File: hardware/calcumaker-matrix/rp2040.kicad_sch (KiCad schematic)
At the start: 22 parts, among them J4 USB-C (BOOTSEL), SW1 BOOTSEL, U1 RP2040, U2 W25Q32JVSSIQ, U3 USBLC6-2SC6, Y1 12MHz

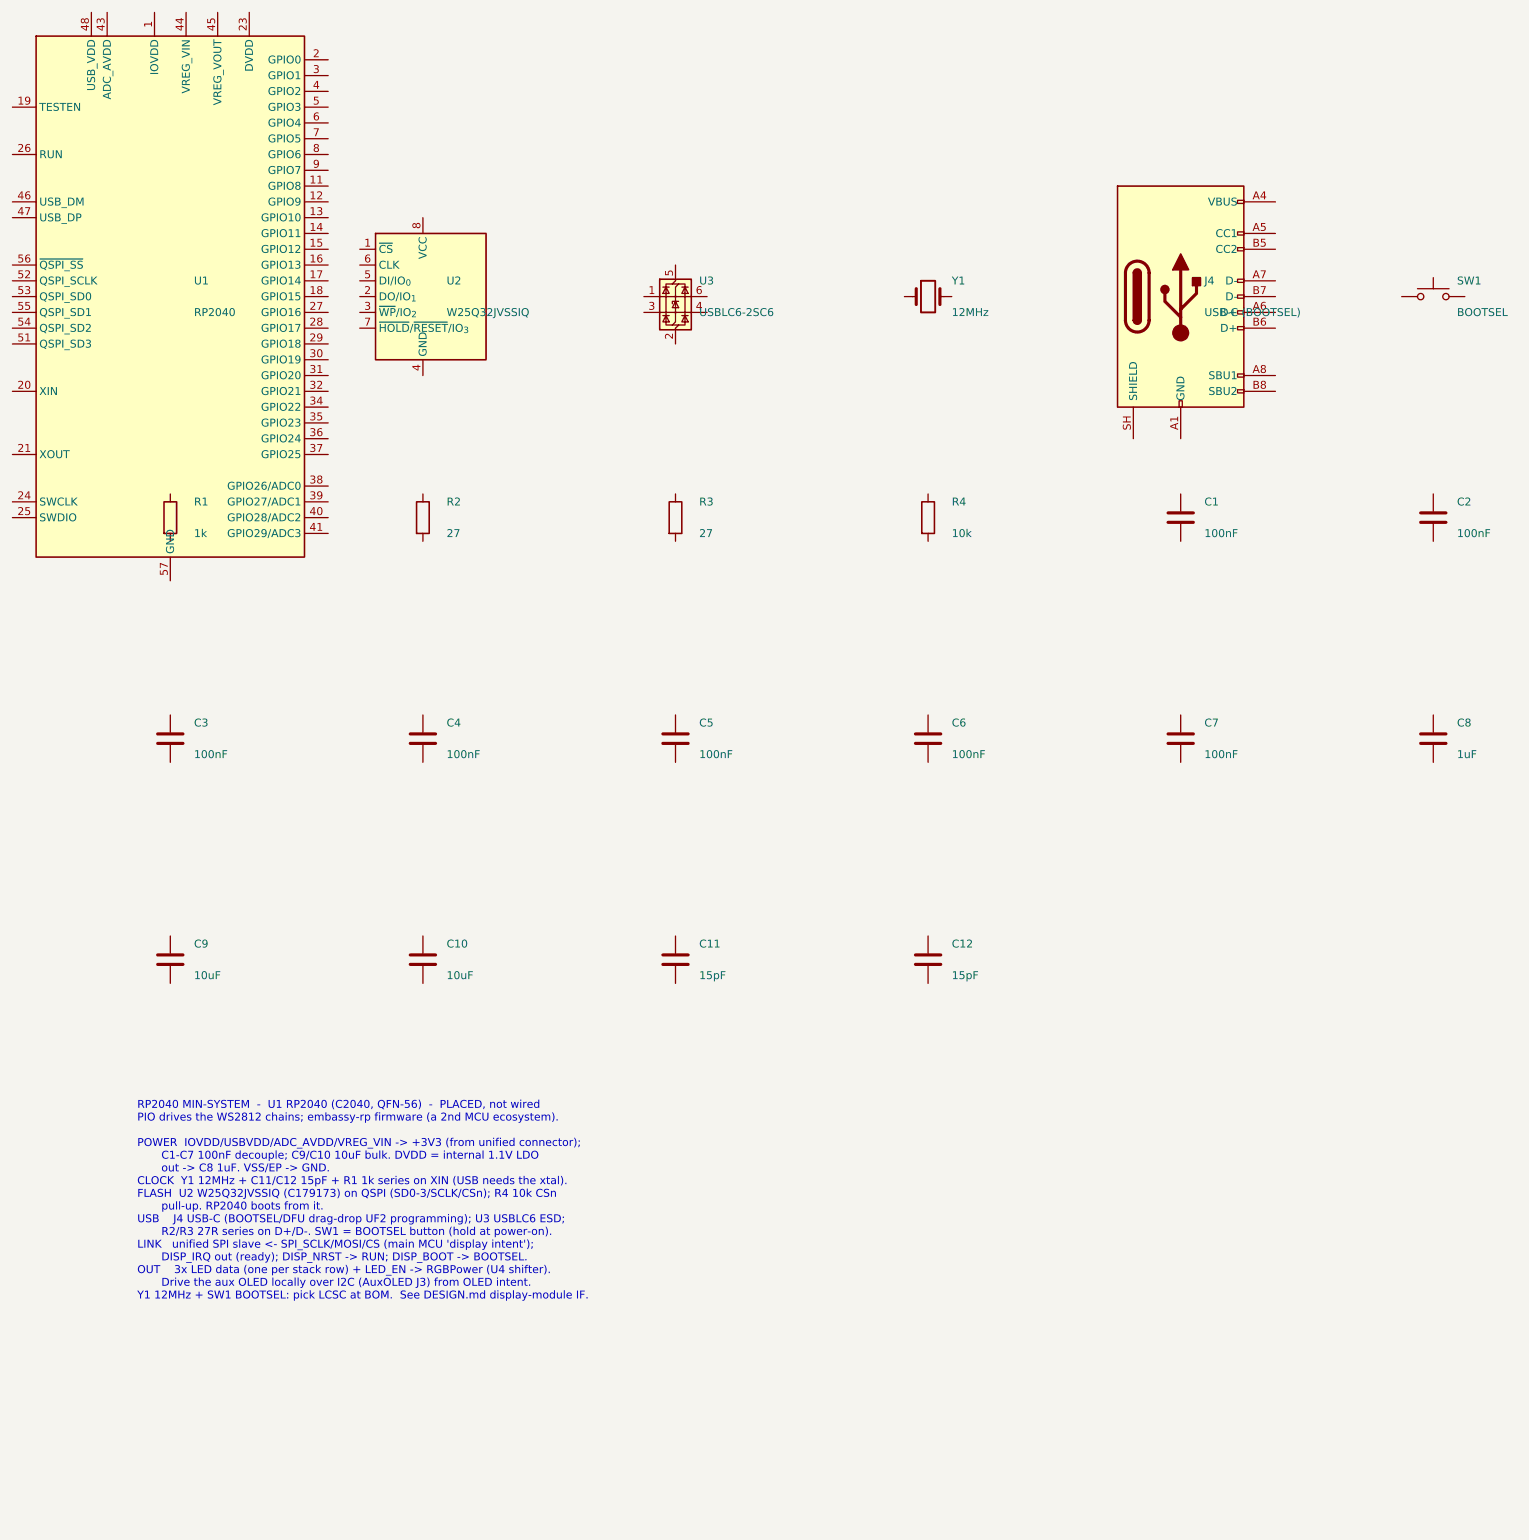
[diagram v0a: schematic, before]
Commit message: firmware: scaffold the two display-module targets + wire the module sheets
Firmware scaffold (all build; targets thumbv6m-none-eabi):
- calcumaker-display-proto: shared no_std wire protocol — the "display intent"
  DisplayFrame the U575 sends over SPI (text rows + flags + aux), with a
  fixed-length checksummed codec. Host-tested (cargo test: 3/3).
- calcumaker-display-fw: 7-seg module (STM32G031, embassy-stm32) — SPI-slave
  receiver + a bit-bang TM1640 driver + 7-seg render.
- calcumaker-matrix-fw: RGB-matrix module (RP2040, embassy-rp) — SPI-slave
  receiver + a 96x24 framebuffer/font blitter; WS2812 PIO output + SPI DMA
  stubbed as the bring-up TODOs.

Wire the one-off module schematic sheets (were placed-not-wired):
- kschgen: pin_geom now follows (extends ...) like pin_numbers, so derived
  symbols (STM32G031, 74xx) wire via net_pin.
- matrix rp2040 + rgb_power: RP2040 power/clock/flash/USB + the FET load switch
  and 3x single-gate level shifters are fully wired.
- display disp_mcu + disp_power: STM32G031 + the TPS61022 boost and 4x single-
  gate shifters are fully wired. (Quad 74xx buffers were multi-unit, which
  kschgen can't place fully, so the shifters are single-gate 74x1G125 — matching
  the keyboard's approach.)

All 4 boards check clean (mcu 46 / keyboard 179 / display 83 / matrix 2343, no
dup refs); wiring cut ERC pin_not_connected ~4x on both display modules.

Co-Authored-By: Claude Opus 4.8 (1M context) <noreply@anthropic.com>
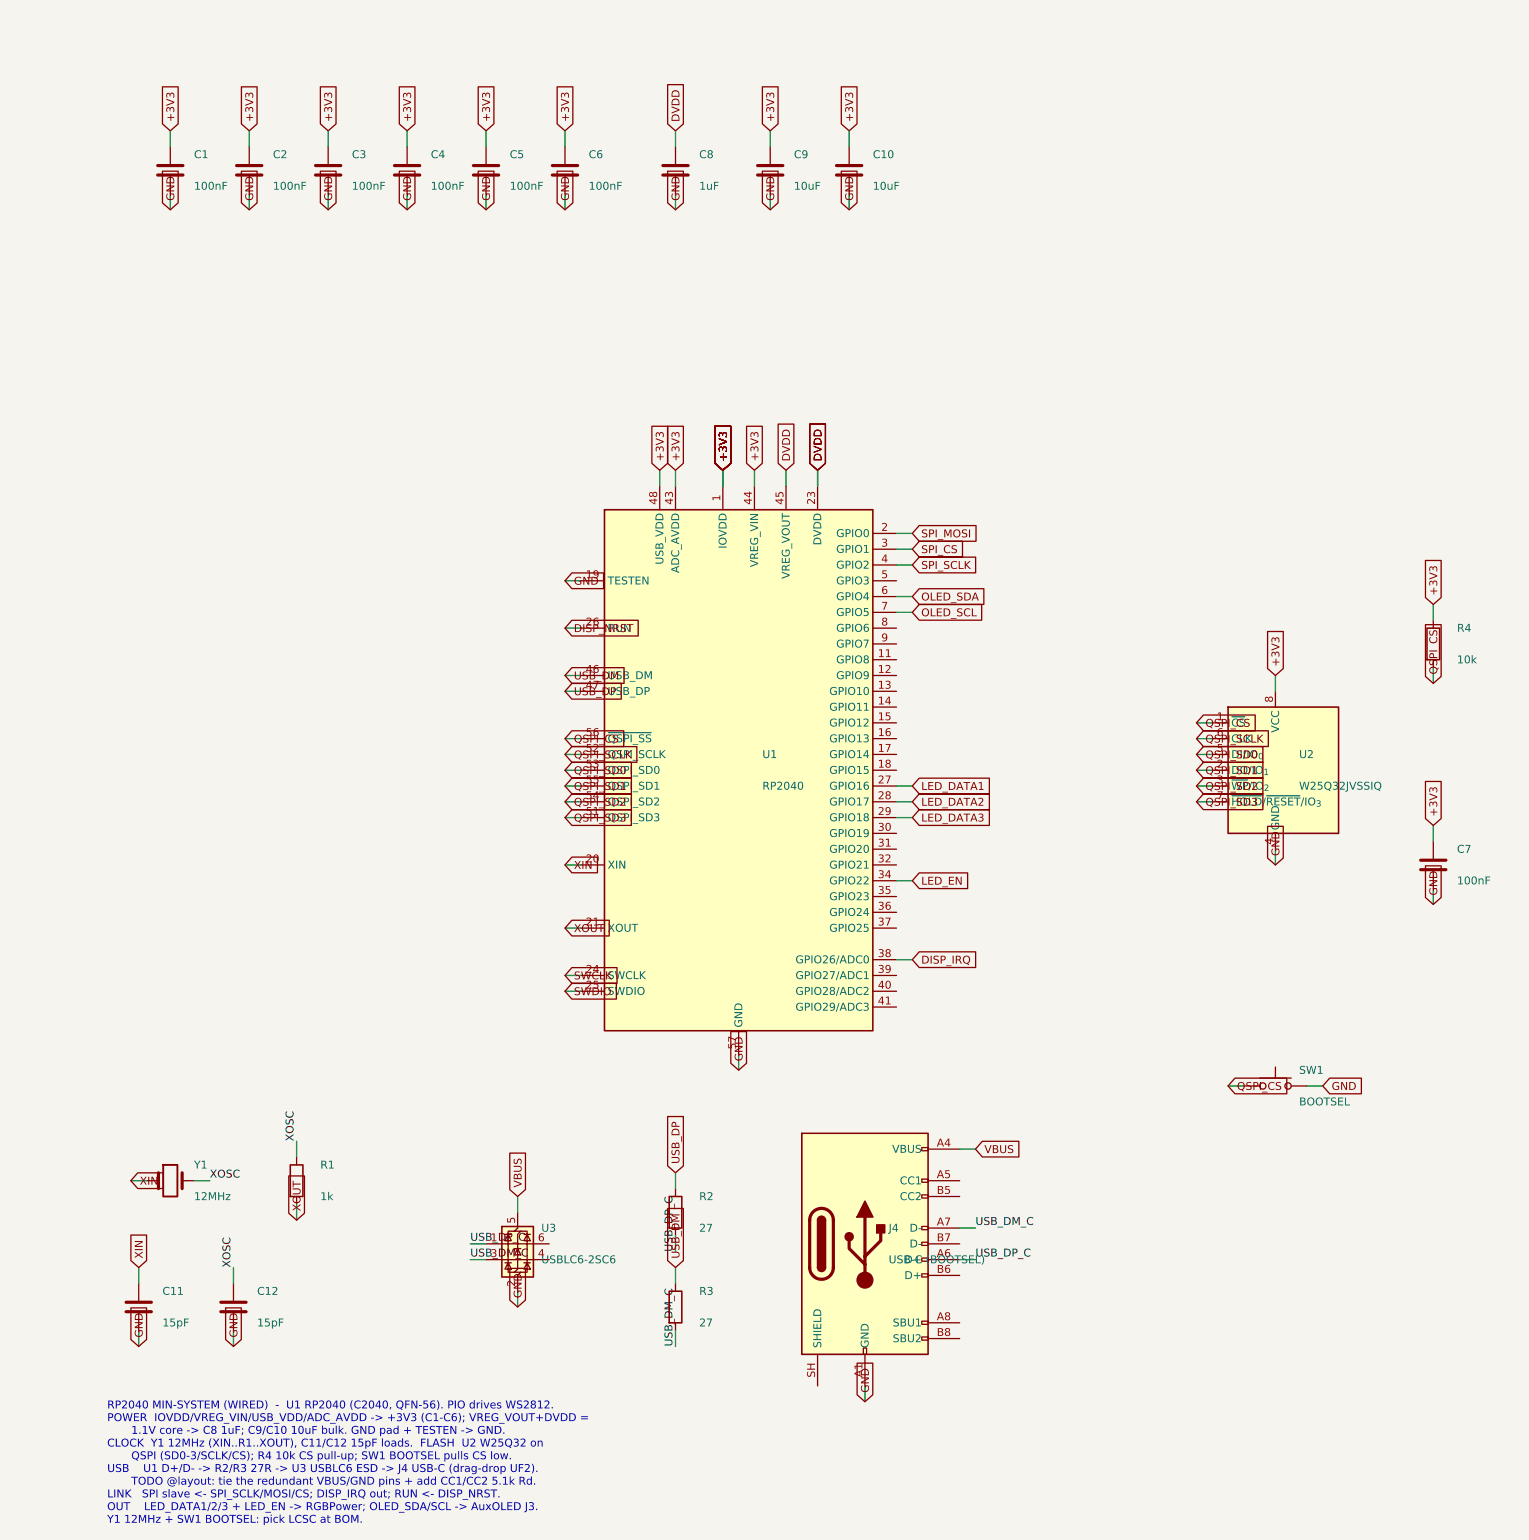
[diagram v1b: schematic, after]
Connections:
- net QSPI_CS: now reaches U2.1 (~{CS})
- net QSPI_CS: now also R4.2, SW1.1, U1.56 (~{QSPI_SS})
- net QSPI_SD1: now reaches U2.2 (DO/IO_{1})
- net QSPI_SD1: now also U1.55 (QSPI_SD1)
- net QSPI_SD2: now reaches U2.3 (~{WP}/IO_{2})
- net QSPI_SD2: now also U1.54 (QSPI_SD2)
- net GND: now reaches U2.4 (GND)
- net GND: now also C1.2, C10.2, C11.2, C12.2, C2.2, C3.2, C4.2, C5.2, C6.2, C7.2, C8.2, C9.2, J4.A1 (GND), J4.A12 (GND), J4.B1 (GND), J4.B12 (GND), SW1.2, U1.19 (TESTEN), U1.57 (GND), U3.2 (GND)
- net QSPI_SD0: now reaches U2.5 (DI/IO_{0})
- net QSPI_SD0: now also U1.53 (QSPI_SD0)
- net QSPI_SCLK: now reaches U2.6 (CLK)
- net QSPI_SCLK: now also U1.52 (QSPI_SCLK)
- net QSPI_SD3: now reaches U2.7 (~{HOLD}/~{RESET}/IO_{3})
- net QSPI_SD3: now also U1.51 (QSPI_SD3)
- net +3V3: now reaches U2.8 (VCC)
- net +3V3: now also C1.1, C10.1, C2.1, C3.1, C4.1, C5.1, C6.1, C7.1, C9.1, R4.1, U1.1 (IOVDD), U1.10 (IOVDD), U1.22 (IOVDD), U1.33 (IOVDD), U1.42 (IOVDD), U1.43 (ADC_AVDD), U1.44 (VREG_VIN), U1.48 (USB_VDD), U1.49 (IOVDD)
- net XIN: now reaches Y1.1
- net XIN: now also C11.1, U1.20 (XIN)
- net XOSC: now reaches Y1.2
- net XOSC: now also C12.1, R1.1
- net USB_DP: now reaches R2.1
- net USB_DP: now also U1.47 (USB_DP)
- net USB_DP_C: now reaches R2.2
- net USB_DP_C: now also J4.A6 (D+), U3.1 (I/O1)
- net USB_DM_C: now reaches U3.3 (I/O2)
- net USB_DM_C: now also J4.A7 (D-), R3.2
- net VBUS: now reaches U3.5 (VBUS)
- net VBUS: now also J4.A4 (VBUS), J4.A9 (VBUS), J4.B4 (VBUS), J4.B9 (VBUS)
- net SPI_MOSI: now reaches U1.2 (GPIO0)
- net XOUT: now reaches U1.21 (XOUT)
- net XOUT: now also R1.2
- net DVDD: now reaches U1.23 (DVDD), U1.50 (DVDD)
- net DVDD: now also C8.1, U1.45 (VREG_VOUT)
- net SWCLK: now reaches U1.24 (SWCLK)
- net SWDIO: now reaches U1.25 (SWDIO)
- net DISP_NRST: now reaches U1.26 (RUN)
- net LED_DATA1: now reaches U1.27 (GPIO16)
- net LED_DATA2: now reaches U1.28 (GPIO17)
- net LED_DATA3: now reaches U1.29 (GPIO18)
- net SPI_CS: now reaches U1.3 (GPIO1)
- net LED_EN: now reaches U1.34 (GPIO22)
- net DISP_IRQ: now reaches U1.38 (GPIO26/ADC0)
- net SPI_SCLK: now reaches U1.4 (GPIO2)
- net USB_DM: now reaches U1.46 (USB_DM)
- net USB_DM: now also R3.1
- net OLED_SDA: now reaches U1.6 (GPIO4)
- net OLED_SCL: now reaches U1.7 (GPIO5)
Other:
- note added: "RP2040 MIN-SYSTEM (WIRED) - U1 RP2040 (C2040, QFN-56). PIO drives WS2812. POWER IOVDD/VREG_VIN/USB_VDD/ADC_AVDD -> +3V3 (C1-C6); VREG_VOUT+DVDD = 1.1V core -> C8 1uF; C9/C10 10uF bulk. GND pad + TESTEN -> GND. CLOCK Y1 12MHz (XIN..R1..XOUT), C11/C12 15pF loads. FLASH U2 W25Q32 on QSPI (SD0-3/SCLK/CS); R4 10k CS pull-up; SW1 BOOTSEL pulls CS low. USB U1 D+/D- -> R2/R3 27R -> U3 USBLC6 ESD -> J4 US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"
- note removed: "RP2040 MIN-SYSTEM - U1 RP2040 (C2040, QFN-56) - PLACED, not wired PIO drives the WS2812 chains; embassy-rp firmware (a 2nd MCU ecosystem). POWER IOVDD/USBVDD/ADC_AVDD/VREG_VIN -> +3V3 (from unified connector); C1-C7 100nF decouple; C9/C10 10uF bulk. DVDD = internal 1.1V LDO out -> C8 1uF. VSS/EP -> GND. CLOCK Y1 12MHz + C11/C12 15pF + R1 1k series on XIN (USB needs the xtal). FLASH U2 W25Q32JVSSI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"
- title: Calcumaker 16 — RGB Matrix — RP2040 min-system (MCU + QSPI flash + USB BOOTSEL) -> Calcumaker 16 — RGB Matrix — RP2040 min-system (MCU + QSPI flash + USB BOOTSEL) — wired
